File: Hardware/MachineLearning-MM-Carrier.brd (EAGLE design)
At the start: 58.4 x 54.6 mm, 126 parts, among them J11 microSD, J2 JTAG, J3 QWIIC_RIGHT_ANGLE, J4 USB-A, J7 CAMERA-HIMAX, J9 MICROMOD-2222-C, U3 AP2127K-1.8V, U4 LIS2DH12, U5 AP7361C-33FGE

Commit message: Update MM connector. Remove backup files. Add ignore.
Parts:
- added J13: (no value), SparkFun-Connectors:1X04_NO_SILK
- J9: device Teensy:M.2-CONNECTOR-E -> SparkFun-MicroMod:M.2-CONNECTOR-E
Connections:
- removed net CAMERA_I2C_SCL: J7.21, J9.53
- removed net CAMERA_I2C_SDA: J7.22, J9.51
- removed net CAMERA_PCLK: J7.17, J9.56
- removed net CAMERA_TRIG: J7.7, J9.67
- removed net D1: J8.6, J9.18
- removed net I2S_SD: E2.6, J9.54
- new net D1/CAMERA_TRIG: J7.7, J8.6, J9.18
- new net I2C_SCL1: J13.4, J9.53
- new net I2C_SDA1: J13.3, J9.51
- new net I2S_SD/CAMERA_PCLK: E2.6, J7.17, J9.54
- net 3.3V: now also J13.2
- net CAMERA_HSYNC: now also J9.65; no longer J9.63
- net CAMERA_MCLK: now also J9.56; no longer J9.58
- net CAMERA_VSYNC: now also J9.63; no longer J9.65
- net GND: now also J13.1
- net I2C_SCL: now also J7.21
- net I2C_SDA: now also J7.22
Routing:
- net D1/CAMERA_TRIG: track 0.00 -> 76.4 mm, vias 0 -> 4
- net D1: track 46.1 -> 0.00 mm, vias 2 -> 0
- net CAMERA_I2C_SCL: track 39.4 -> 0.00 mm, vias 2 -> 0
- net CAMERA_I2C_SDA: track 38.3 -> 0.00 mm, vias 2 -> 0
- net I2C_SCL1: track 0.00 -> 38.0 mm, vias 0 -> 2
- net CAMERA_PCLK: track 37.9 -> 0.00 mm, vias 2 -> 0
- net I2C_SDA1: track 0.00 -> 37.5 mm, vias 0 -> 2
- net CAMERA_MCLK: track 39.6 -> 74.8 mm, vias 2 -> 4
- net CAMERA_TRIG: track 32.0 -> 0.00 mm, vias 2 -> 0
- net I2S_SD/CAMERA_PCLK: track 0.00 -> 21.7 mm, vias 0 -> 2
- net I2S_SD: track 21.7 -> 0.00 mm, vias 2 -> 0
- net CAMERA_HSYNC: track 33.8 -> 31.4 mm
- net CAMERA_VSYNC: track 31.7 -> 30.3 mm

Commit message: v11 routed
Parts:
- removed J12: (no value), SparkFun-Connectors:1X03_NO_SILK
- removed J13: (no value), SparkFun-Connectors:1X04_NO_SILK
- removed J4: USB-A, SparkFun-Connectors:USB-A-S-SILK-FEMALE
- removed U$23, U$33: (no value), SparkFun-Buzzard:GND_P
- removed U$28, U$56: (no value), buzzard_labels (12):TX24
- removed U$30: (no value), buzzard_labels (12):RX25
- added D2: RED, SparkFun-LED:LED-0603
- added JP4: (no value), SparkFun-Jumpers:SMT-JUMPER_2_NC_TRACE_SILK
- added R11: 1k, SparkFun-Resistors:0603
- U$17: device buzzard_labels (12):RX25 -> SparkFun-Buzzard:PWR
- U$20: device buzzard_labels (10):USB_HOST0 -> SparkFun-Buzzard:PWR_TO
- moved J6 47.2 mm to (1.27, 29.2), flipped to the bottom, turned to 270 degrees
- moved U$41 46.9 mm to (1.52, 29.2), flipped to the top, turned to 0 degrees
- moved U$31 43.3 mm to (6.10, 29.2), flipped to the bottom, turned to 0 degrees
- moved U$25 43.2 mm to (1.65, 26.7), flipped to the top, turned to 0 degrees
- moved U$29 39.7 mm to (5.97, 26.7), flipped to the bottom, turned to 0 degrees
- moved U$42 39.6 mm to (1.65, 24.1), flipped to the top, turned to 0 degrees
- moved U$32 35.8 mm to (6.48, 24.1), flipped to the bottom, turned to 0 degrees
- moved U$54 28.4 mm to (57.1, 45.0), turned to 270 degrees
- moved J14 27.5 mm to (57.1, 24.1), flipped to the bottom, turned to 270 degrees
- moved U$36 26.9 mm to (56.8, 24.1), flipped to the bottom, turned to 0 degrees
- moved U$45 24.6 mm to (51.9, 24.1), flipped to the top, turned to 0 degrees
- moved U$11 23.6 mm to (57.1, 40.1)
- moved U$38 23.6 mm to (56.9, 21.6), flipped to the bottom, turned to 0 degrees
- moved U$46 21.5 mm to (52.2, 21.6), flipped to the top, turned to 0 degrees
- moved U$39 20.1 mm to (56.9, 19.1), flipped to the bottom, turned to 0 degrees
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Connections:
- removed net I2C_SCL1: J13.4, J9.53
- removed net I2C_SDA1: J13.3, J9.51
- removed net RX2: J12.2, J9.20
- removed net TX2: J12.1, J9.22
- removed net USBHOST_D+: J4.D+, J9.35
- removed net USBHOST_D-: J4.D-, J9.37
- new net N$6: JP4.1, R11.2
- new net N$7: D2.A, R11.1
- net 3.3V: now also JP4.2; no longer J13.2
- net GND: now also D2.C; no longer J12.3, J13.1, J4.GND
- net V_USB: no longer J4.VBUS
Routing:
- net I2C_SCL: track 48.4 -> 89.1 mm, vias 0 -> 3
- net I2C_SCL1: track 38.0 -> 0.00 mm, vias 2 -> 0
- net I2C_SDA1: track 37.5 -> 0.00 mm, vias 2 -> 0
- net CAMERA_MCLK: track 74.8 -> 37.5 mm, vias 4 -> 2
- net I2S_SD/CAMERA_PCLK: track 21.7 -> 57.6 mm, vias 2 -> 4
- net I2C_SDA: track 52.0 -> 87.4 mm, vias 0 -> 3
- net USBHOST_D-: track 23.2 -> 0.00 mm, vias 2 -> 0
- net 3.3V: track 205.2 -> 227.6 mm, vias 10 -> 11
- net USBHOST_D+: track 20.7 -> 0.00 mm, vias 2 -> 0
- net TX2: track 20.4 -> 0.00 mm, vias 1 -> 0
- net V_USB: track 38.4 -> 18.7 mm
- net RX2: track 19.0 -> 0.00 mm, vias 1 -> 0
- net RX1: track 32.1 -> 25.4 mm
- net SPI_CLK: track 37.5 -> 31.1 mm, vias 2 -> 1
- net SPI_!CS!: track 32.0 -> 26.4 mm, vias 2 -> 1
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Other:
- board size 58.4 x 54.6 mm -> 58.4 x 52.1 mm
- board text added: "v11"
- board text removed: "x01"

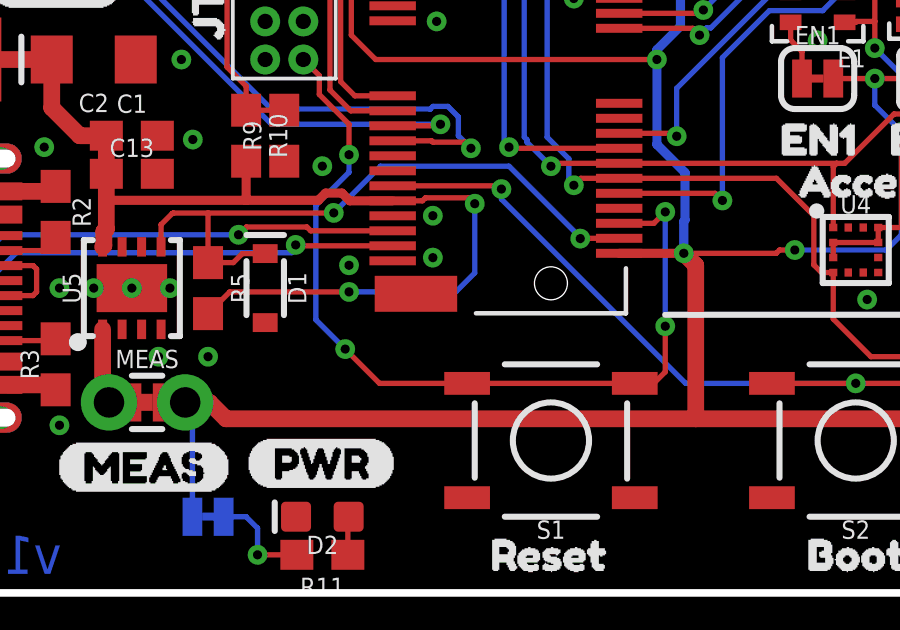
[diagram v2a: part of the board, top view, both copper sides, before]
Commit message: Change RTC charge to 3.3k. Add bulk cap to vreg output.
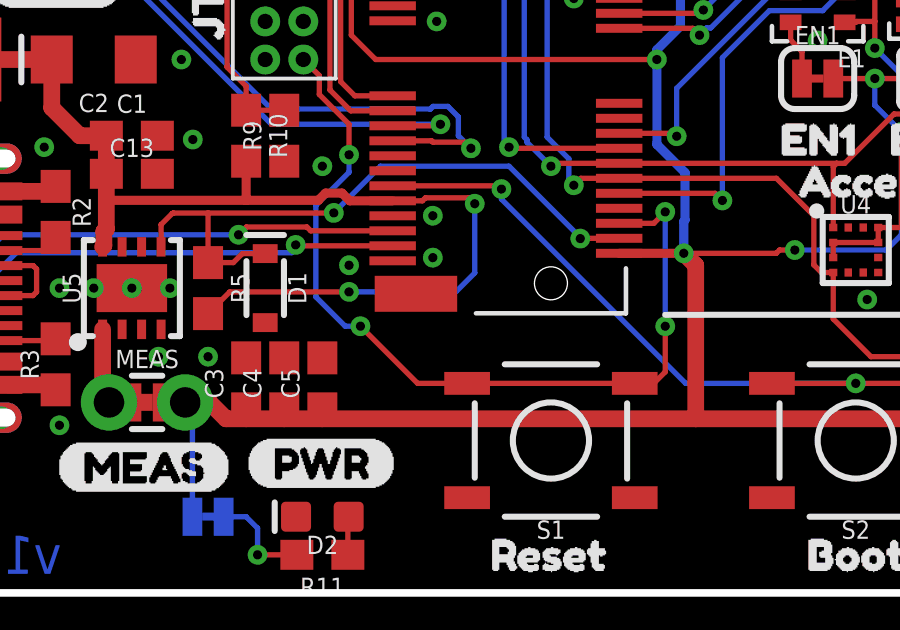
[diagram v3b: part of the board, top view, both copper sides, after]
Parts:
- added C3: 1.0uF, SparkFun-Capacitors:0603
- added C4: 0.1uF, SparkFun-Capacitors:0603
- added C5: 0.22uF, SparkFun-Capacitors:0603
- R8: value 1k -> 3.3k
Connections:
- net 3.3V: now also C3.1, C4.1, C5.1
- net GND: now also C3.2, C4.2, C5.2
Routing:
- net 3.3V: track 227.6 -> 228.5 mm

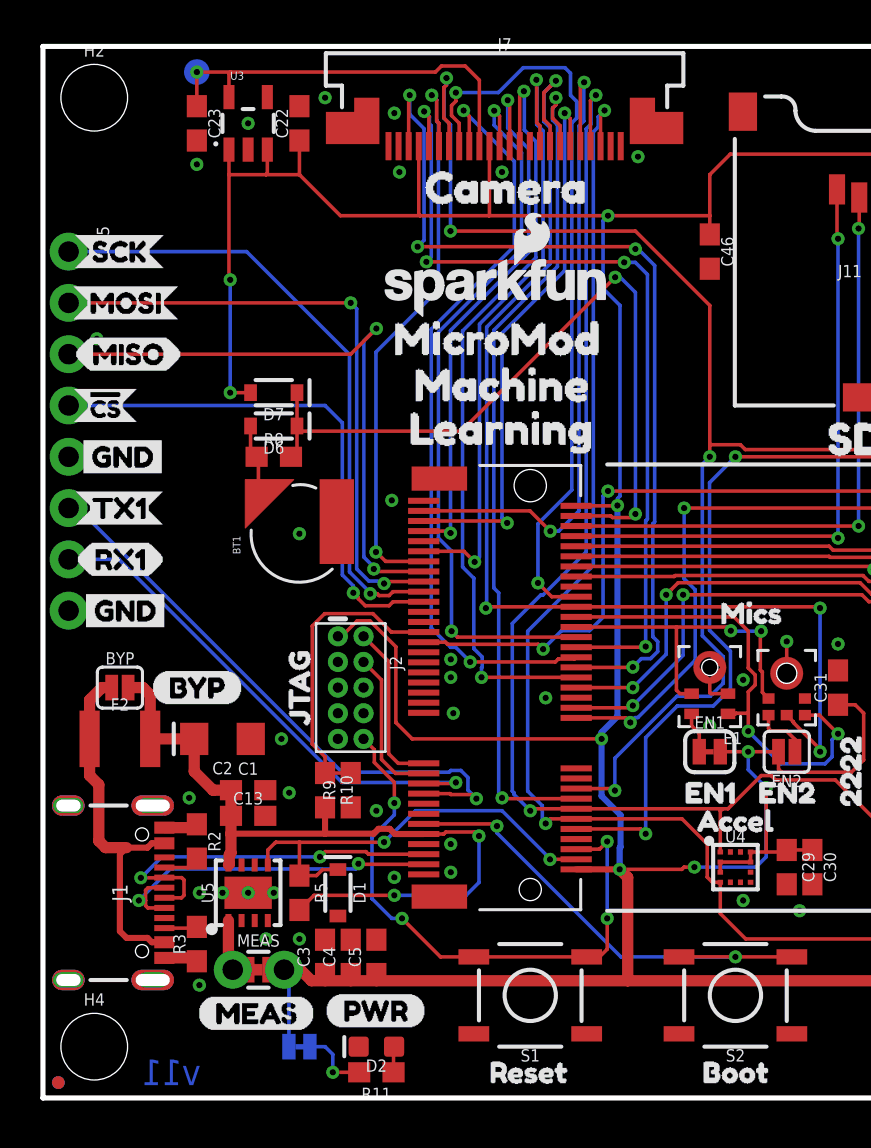
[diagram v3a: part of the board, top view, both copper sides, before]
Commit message: Update micromod connector to new SPI pinout
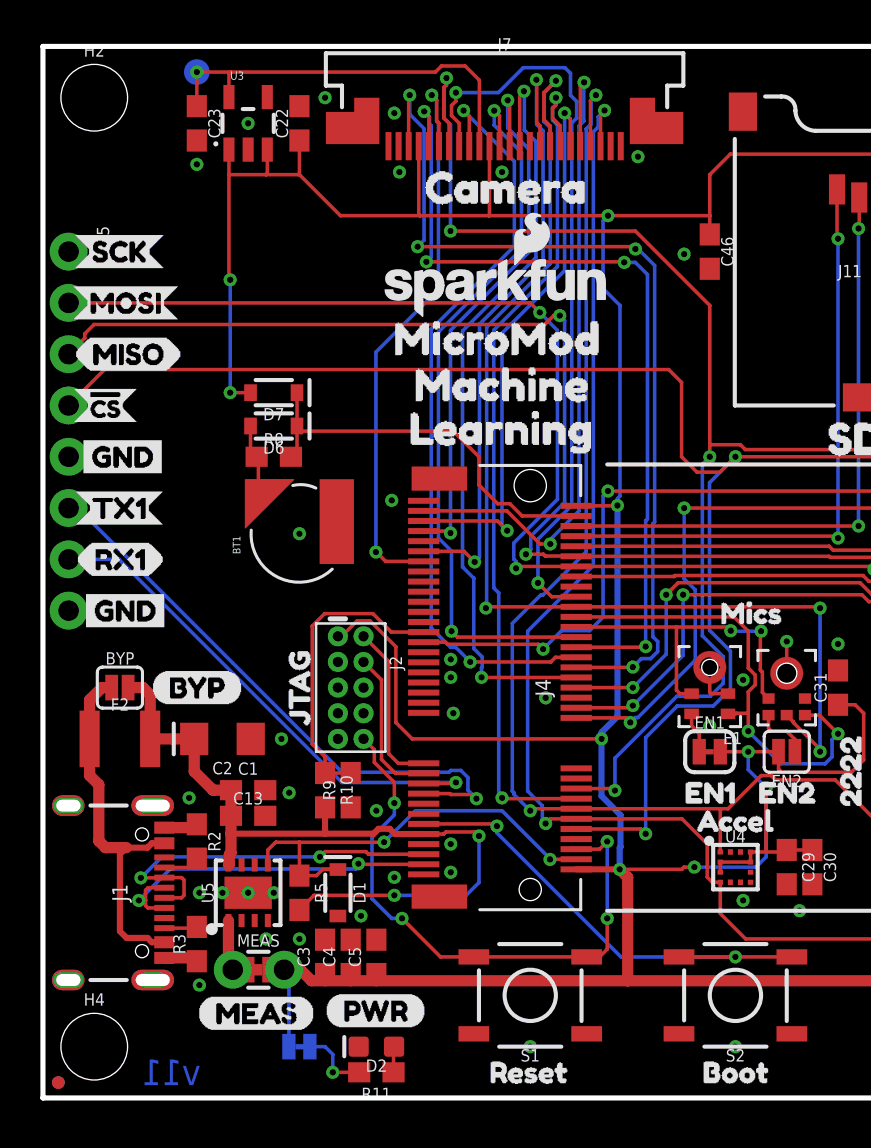
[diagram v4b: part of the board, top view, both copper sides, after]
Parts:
- renumbered J9 to J4
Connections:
- net SD_CLK renamed SPI_SCK
- net SD_DAT3 renamed SD_!CS!
- removed net D0: J4.10, J8.5
- removed net SD_CMD: J11.DI, J4.62
- removed net SD_DAT0: J11.DO, J4.64
- removed net SPI_!CS!: J4.55, J5.4
- new net HEADER_!CS!: J4.10, J5.4, J8.5
- net SPI_CLK: no longer J4.57
- net SPI_MISO: now also J11.DO, J4.64; no longer J4.61
- net SPI_MOSI: now also J11.DI, J4.62; no longer J4.59
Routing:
- net HEADER_!CS!: track 0.00 -> 86.7 mm, vias 0 -> 2
- net D0: track 48.4 -> 0.00 mm, vias 2 -> 0
- net SPI_MISO: track 30.7 -> 78.7 mm, vias 2 -> 4
- net SPI_MOSI: track 30.9 -> 74.3 mm, vias 2 -> 4
- net SD_DAT0: track 38.2 -> 0.00 mm, vias 2 -> 0
- net SD_CMD: track 33.8 -> 0.00 mm, vias 2 -> 0
- net SPI_CLK: track 31.1 -> 0.00 mm, vias 1 -> 0
- net SPI_!CS!: track 26.4 -> 0.00 mm, vias 1 -> 0
- net RTC_3V: track 37.7 -> 19.9 mm, vias 2 -> 0
- net CAMERA_D5: track 33.1 -> 33.7 mm
- net CAMERA_D6: track 27.6 -> 28.1 mm
- net GND: vias 36 -> 39

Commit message: Fix route to SPI SCK
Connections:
- removed net SPI_CLK: J5.1
- net SPI_SCK: now also J5.1
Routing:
- net SPI_SCK: track 36.9 -> 82.4 mm, vias 2 -> 3
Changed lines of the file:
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@@
 <layer number="47" name="Measures" color="7" fill="1" visible="no" active="yes"/>
 <layer number="48" name="Document" color="7" fill="1" visible="no" active="yes"/>
-<layer number="49" name="Reference" color="7" fill="1" visible="yes" active="yes"/>
+<layer number="49" name="Reference" color="7" fill="1" visible="no" active="yes"/>
 <layer number="50" name="dxf" color="7" fill="1" visible="no" active="yes"/>
 <layer number="51" name="tDocu" color="6" fill="1" visible="yes" active="yes"/>
@@
 <wire x1="40.90075" y1="25.5768" x2="43.6382" y2="25.5768" width="0.1778" layer="1"/>
 <wire x1="40.60815" y1="25.8694" x2="40.90075" y2="25.5768" width="0.1778" layer="1"/>
-<wire x1="31.292625" y1="25.857375" x2="31.30465" y2="25.8694" width="0.1778" layer="1"/>
 <wire x1="31.30465" y1="25.8694" x2="40.60815" y2="25.8694" width="0.1778" layer="1"/>
 <wire x1="43.72" y1="44.99" x2="43.72" y2="43.085" width="0.1778" layer="1"/>
@@
 <contactref element="J4" pad="60"/>
 <wire x1="26.405" y1="25.82" x2="31.25525" y2="25.82" width="0.1778" layer="1"/>
-<wire x1="31.25525" y1="25.82" x2="31.292625" y2="25.857375" width="0.1778" layer="1"/>
+<wire x1="31.25525" y1="25.82" x2="31.30465" y2="25.8694" width="0.1778" layer="1"/>
+<contactref element="J5" pad="1"/>
+<via x="31.75" y="39.37" extent="1-16" drill="0.3048"/>
+<wire x1="1.27" y1="41.91" x2="6.97596875" y2="41.91" width="0.254" layer="1"/>
+<wire x1="6.97596875" y1="41.91" x2="9.00796875" y2="39.878" width="0.254" layer="1"/>
+<wire x1="31.242" y1="39.878" x2="31.75" y2="39.37" width="0.254" layer="1"/>
+<wire x1="9.00796875" y1="39.878" x2="31.242" y2="39.878" width="0.254" layer="1"/>
+<wire x1="31.75" y1="39.37" x2="35.29696875" y2="39.37" width="0.254" layer="16"/>
+<wire x1="42.17303125" y1="43.053" x2="43.688" y2="43.053" width="0.254" layer="16"/>
+<wire x1="35.29696875" y1="39.37" x2="39.61496875" y2="43.688" width="0.254" layer="16"/>
+<wire x1="39.61496875" y1="43.688" x2="41.53803125" y2="43.688" width="0.254" layer="16"/>
+<wire x1="41.53803125" y1="43.688" x2="42.17303125" y2="43.053" width="0.254" layer="16"/>
 </signal>
 <signal name="SPI_MOSI">
@@
 <wire x1="17.36" y1="2.513" x2="17.387" y2="2.54" width="0.1778" layer="1"/>
 </signal>
-<signal name="SPI_CLK">
-<contactref element="J5" pad="1"/>
-</signal>
 <signal name="HEADER_!CS!">

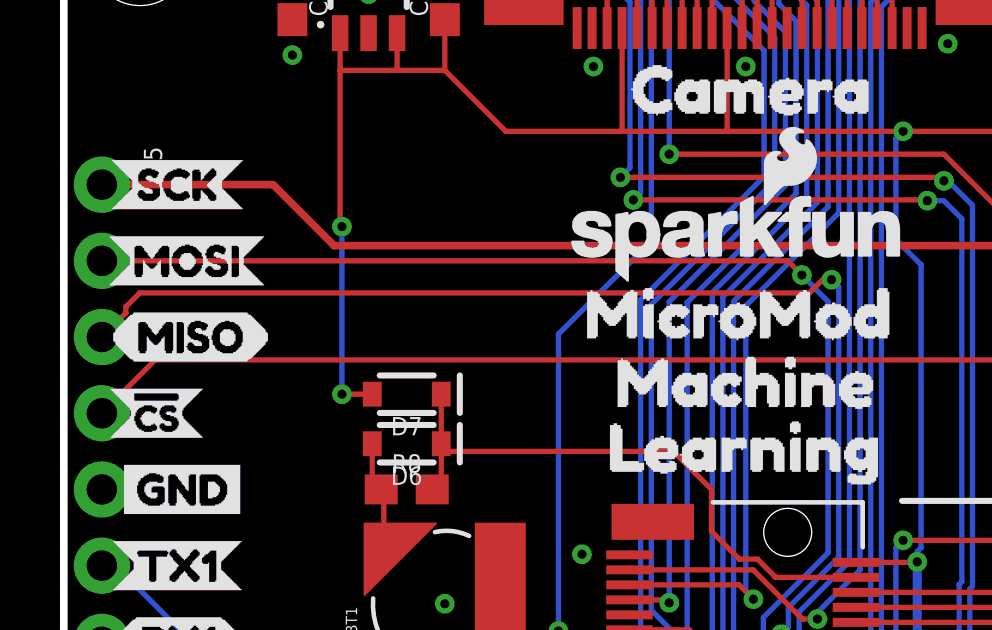
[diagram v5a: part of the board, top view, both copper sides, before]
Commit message: Update v-reg device
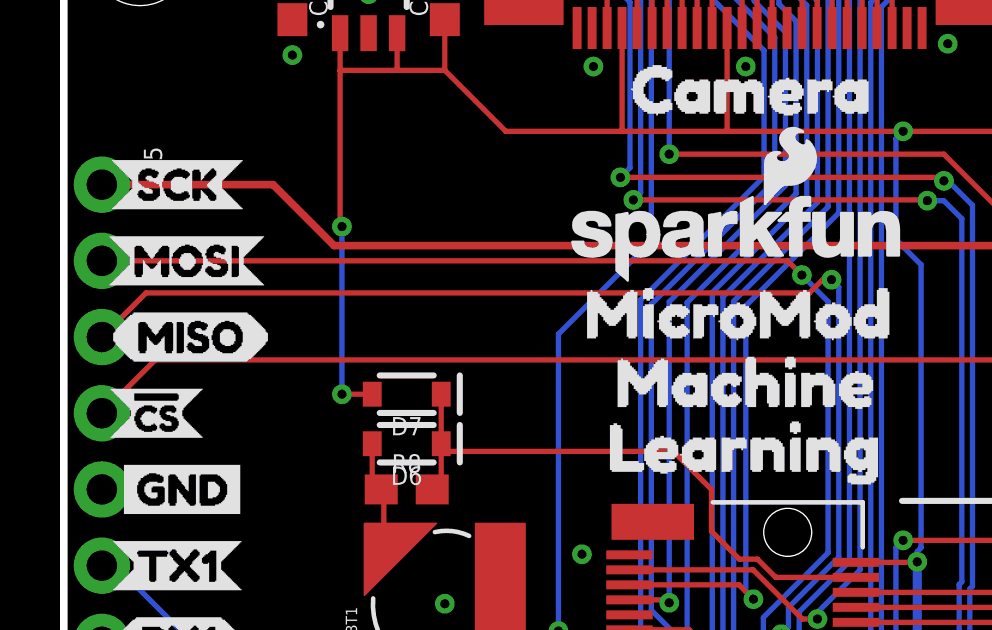
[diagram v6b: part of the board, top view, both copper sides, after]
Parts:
- U5: device ublox:8-UDFN -> SparkFun-IC-Power:UDFN-8
